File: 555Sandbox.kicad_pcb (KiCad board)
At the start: 2 copper layers, 64.6 x 37 mm, 33 parts, among them J1 VIN, J2 Piezo, SW1 RESET, SW2 MODE, U1 NE555P, U2 LM3914N

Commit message: patch: silkscreen updates
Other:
- board text added: "555"
- board text added: "VOLT- METER"
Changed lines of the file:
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@@
 			(at 4.01 -2.3 180)
 			(layer "F.SilkS")
+			(hide yes)
 			(effects
 				(font
@@
 	(footprint "Potentiometer_THT:Potentiometer_Alps_RK163_Single_Horizontal"
 		(layer "F.Cu")
-		(at 89.6 68.75 -90)
+		(at 89.55 68.75 -90)
 		(descr "1110U1Q 1110TNP 1110U2A 1110U0Q Potentiometer, horizontal, Alps RK163 Single, https://tech.alpsalpine.com/prod/e/pdf/potentiometer/rotarypotentiometers/rk16/rk16.pdf")
 		(tags "Potentiometer horizontal Alps RK163 Single")
@@
 			)
 		)
-		(property ki_fp_filters "Potentiometer*")
-		(sheetname "Root")
-		(sheetfile "555Sandbox.kicad_sch")
 		(attr through_hole)
 		(fp_line
 			(start 6.82 14.07)
-			(end -0.92 14.07)
+			(end -0.72 14.07)
 			(stroke
 				(width 0.12)
@@
 		)
 		(fp_line
-			(start -3.92 11.07)
+			(start -3.92 10.87)
 			(end -3.92 -4.07)
 			(stroke
@@
 		)
 		(fp_arc
-			(start -0.92 14.07)
-			(mid -3.04132 13.19132)
-			(end -3.92 11.07)
+			(start -0.72 14.07)
+			(mid -2.982742 13.132742)
+			(end -3.92 10.87)
 			(stroke
 				(width 0.12)
@@
 	)
 	(gr_line
+		(start 117.725 74.55)
+		(end 117 73.85)
+		(stroke
+			(width 0.25)
+			(type default)
+		)
+		(layer "F.SilkS")
+	)
+	(gr_line
 		(start 113.75 71.65)
 		(end 116.75 71.65)
@@
 	)
 	(gr_line
+		(start 104.85 74.55)
+		(end 102.875 74.55)
+		(stroke
+			(width 0.25)
+			(type default)
+		)
+		(layer "F.SilkS")
+	)
+	(gr_line
 		(start 82.2 72.2)
 		(end 82.2 74.1)
@@
 	)
 	(gr_line
-		(start 110.7 80.1)
-		(end 110.7 90)
+		(start 110.35 80.1)
+		(end 110.35 90)
 		(stroke
 			(width 0.2)
@@
 		(layer "F.SilkS")
 	)
+	(gr_line
+		(start 102.875 74.55)
+		(end 103.6 73.85)
+		(stroke
+			(width 0.25)
+			(type default)
+		)
+		(layer "F.SilkS")
+	)
+	(gr_line
+		(start 102.875 74.55)
+		(end 103.6 75.25)
+		(stroke
+			(width 0.25)
+			(type default)
+		)
+		(layer "F.SilkS")
+	)
 	(gr_arc
 		(start 135.8 65.4)
@@
 	)
 	(gr_line
+		(start 116.2 74.55)
+		(end 117.725 74.55)
+		(stroke
+			(width 0.25)
+			(type default)
+		)
+		(layer "F.SilkS")
+	)
+	(gr_line
 		(start 83.6 72.2)
 		(end 84.3 72.2)
@@
 	)
 	(gr_line
-		(start 110.7 72.8)
-		(end 110.7 76.3)
+		(start 110.35 72.8)
+		(end 110.35 76.3)
 		(stroke
 			(width 0.2)
@@
 		(layer "F.SilkS")
 	)
+	(gr_line
+		(start 117.725 74.55)
+		(end 117 75.25)
+		(stroke
+			(width 0.25)
+			(type default)
+		)
+		(layer "F.SilkS")
+	)
 	(gr_arc
 		(start 139.55 97.5)
@@
 		)
 	)
+	(gr_text "555"
+		(at 109.8375 73.75 0)
+		(layer "F.SilkS")
+		(effects
+			(font
+				(size 1.5 1.5)
+				(thickness 0.3)
+				(bold yes)
+			)
+			(justify right top)
+		)
+	)
 	(gr_text "Freq"
 		(at 84.7 74.1 0)
@@
 		)
 	)
+	(gr_text "VOLT-\nMETER"
+		(at 111 76 0)
+		(layer "F.SilkS")
+		(effects
+			(font
+				(size 1 1)
+				(thickness 0.2)
+				(bold yes)
+			)
+			(justify left bottom)
+		)
+	)
 	(gr_text "5-16V"
 		(at 111 72.3 0)
@@
 	)
 	(segment
+		(start 89.55 68.75)
+		(end 89.55 76.15)
+		(width 1)
+		(layer "F.Cu")
+		(net 4)
+	)
+	(segment
 		(start 102.94 84.54)
 		(end 99.08 84.54)
@@
 	)
 	(segment
-		(start 89.6 68.75)
-		(end 89.6 76.2)
+		(start 89.55 76.15)
+		(end 90.9 77.5)
 		(width 1)
 		(layer "F.Cu")
@@
 	)
 	(segment
-		(start 89.6 76.2)
-		(end 90.9 77.5)
-		(width 1)
-		(layer "F.Cu")
-		(net 4)
-	)
-	(segment
-		(start 84.6 68.75)
+		(start 84.55 68.75)
 		(end 89.6 68.75)
 		(width 1)
@@
 		(end 126.5 70.7)
 		(width 1)
-		(layer "F.Cu")
+		(layer "B.Cu")
 		(net 6)
 	)
@@
 		(end 126.52 75.8)
 		(width 1)
-		(layer "F.Cu")
+		(layer "B.Cu")
 		(net 8)
 	)
@@
 		(end 126.54 80.9)
 		(width 1)
-		(layer "F.Cu")
+		(layer "B.Cu")
 		(net 10)
 	)
@@
 		(end 126.54 85.9)
 		(width 1)
-		(layer "F.Cu")
+		(layer "B.Cu")
 		(net 12)
 	)
@@
 	)
 	(segment
-		(start 129.06 91)
-		(end 126.52 91)
-		(width 1)
-		(layer "F.Cu")
-		(net 14)
-	)
-	(segment
 		(start 126.52 91)
 		(end 126.5 91.02)
@@
 	)
 	(segment
+		(start 129.06 91)
+		(end 126.52 91)
+		(width 1)
+		(layer "B.Cu")
+		(net 14)
+	)
+	(segment
 		(start 95.71 83.4)
 		(end 95.71 87.1)
@@
 	)
 	(segment
-		(start 77 71.35)
-		(end 77 82.85)
+		(start 77 82.85)
+		(end 79.4 85.25)
 		(width 1)
 		(layer "B.Cu")
@@
 	)
 	(segment
-		(start 79.6 68.75)
+		(start 79.55 68.8)
 		(end 77 71.35)
 		(width 1)
@@
 	)
 	(segment
-		(start 77 82.85)
-		(end 79.4 85.25)
+		(start 77 71.35)
+		(end 77 82.85)
+		(width 1)
+		(layer "B.Cu")
+		(net 27)
+	)
+	(segment
+		(start 79.55 68.75)
+		(end 79.55 68.8)
 		(width 1)
 		(layer "B.Cu")

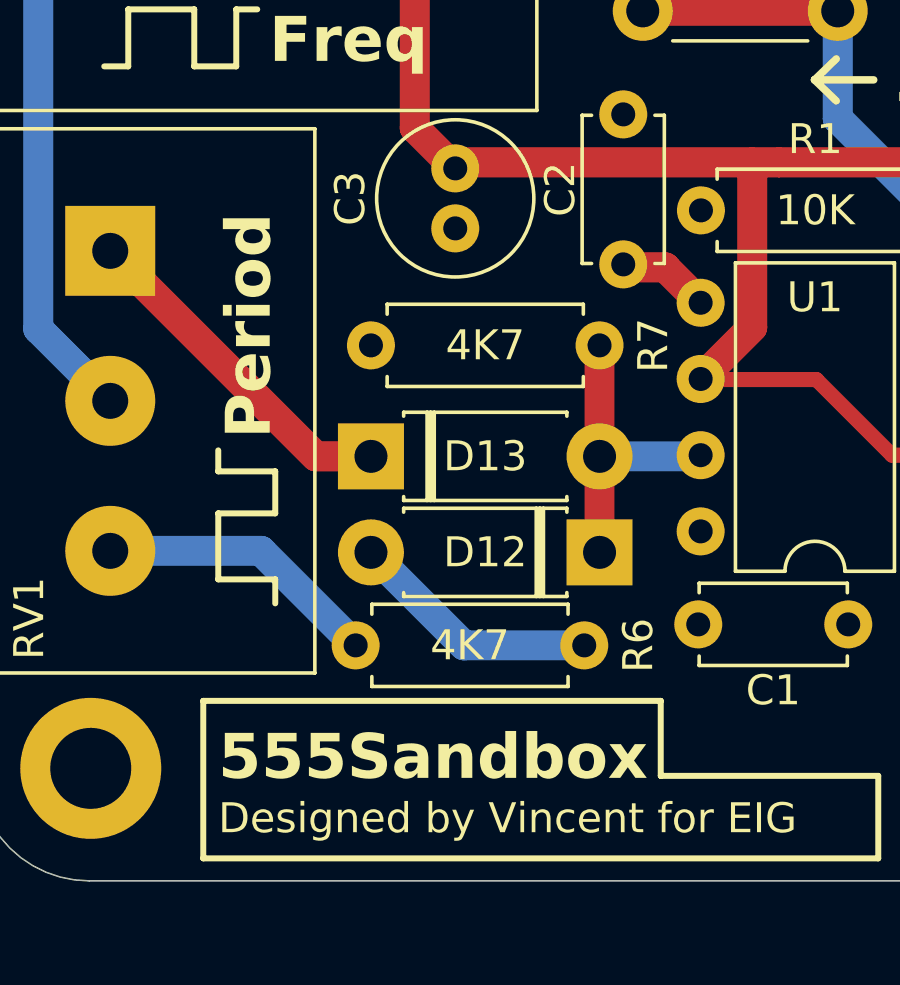
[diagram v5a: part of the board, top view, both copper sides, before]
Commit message: patch: back silkscreen logo additions
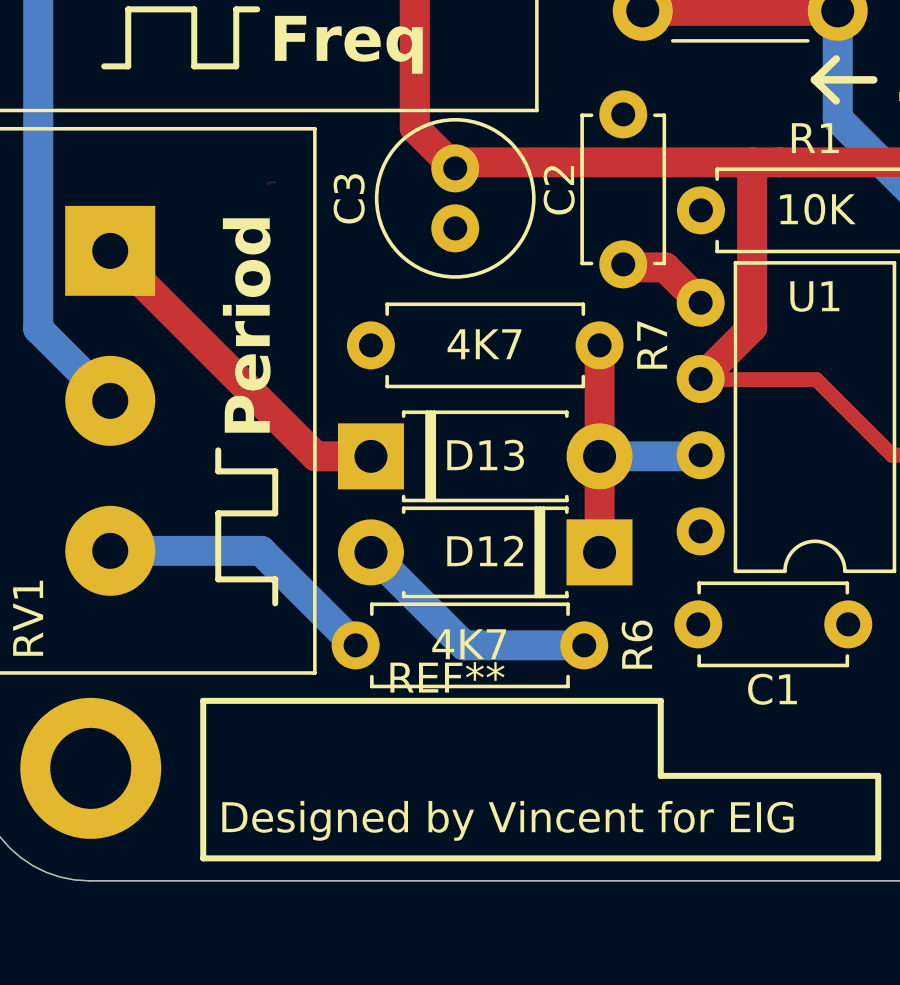
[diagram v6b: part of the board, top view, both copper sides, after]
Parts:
- added G***: LOGO, footprints:Bear_40, F.Cu at (86.5, 80.2)
- added REF**: EIG, footprints:EIG, F.Cu at (90.6, 95.0)

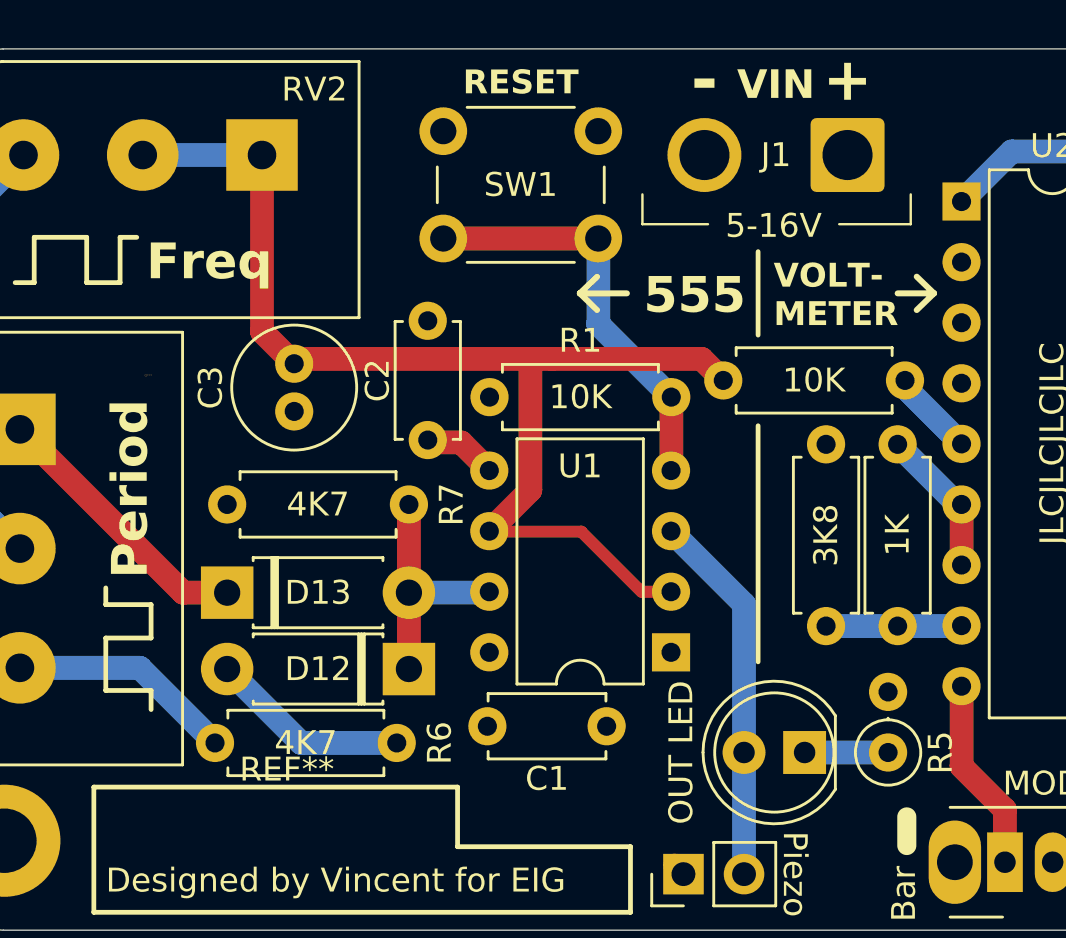
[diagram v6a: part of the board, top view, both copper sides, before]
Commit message: fix: polarised capacitor and erronous silkscreen label
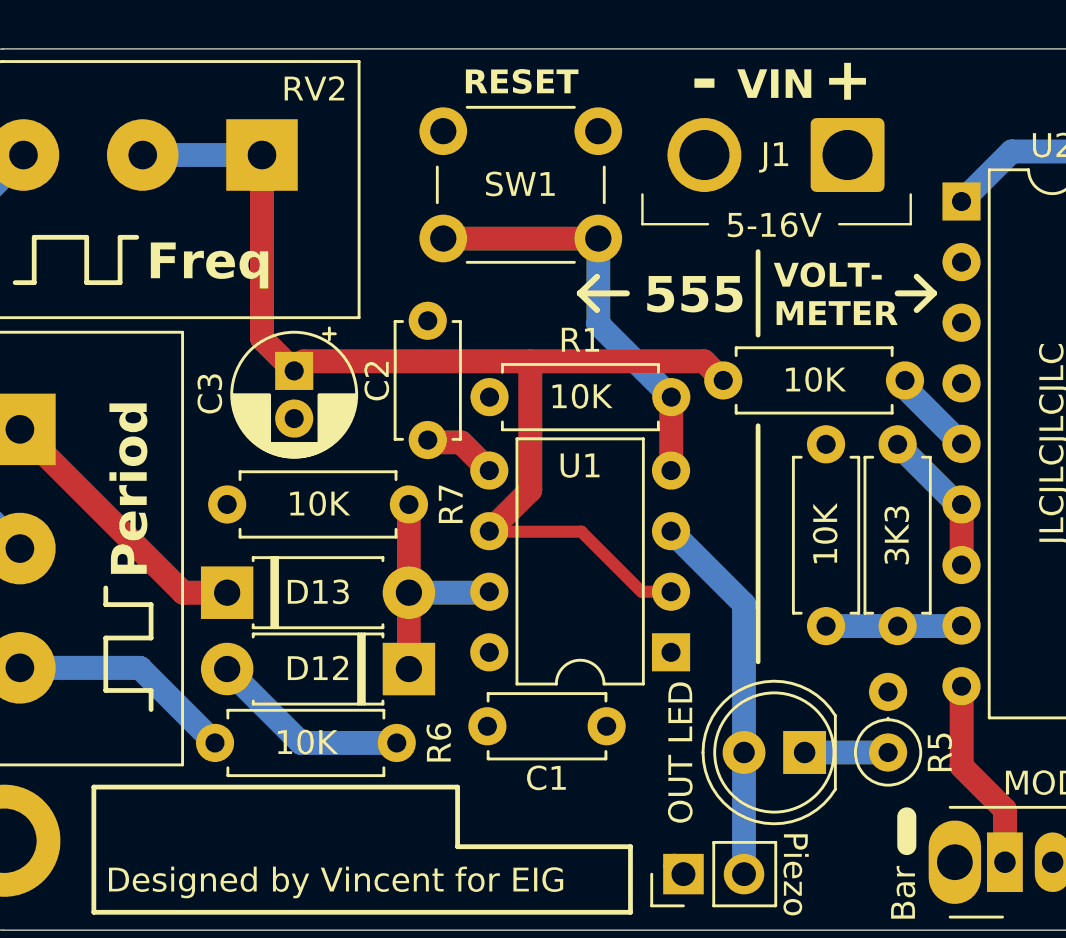
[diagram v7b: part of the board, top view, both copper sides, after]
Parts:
- removed REF**: EIG, footprints:EIG
- C3: footprint Capacitor_THT:C_Radial_D5.0mm_H11.0mm_P2.00mm -> Capacitor_THT:CP_Radial_D5.0mm_P2.00mm
- R2: value 1K -> 3K3
- R4: value 3K8 -> 10K
- R6, R7: value 4K7 -> 10K
- moved C3 0.30 mm to (90.9, 77.8)

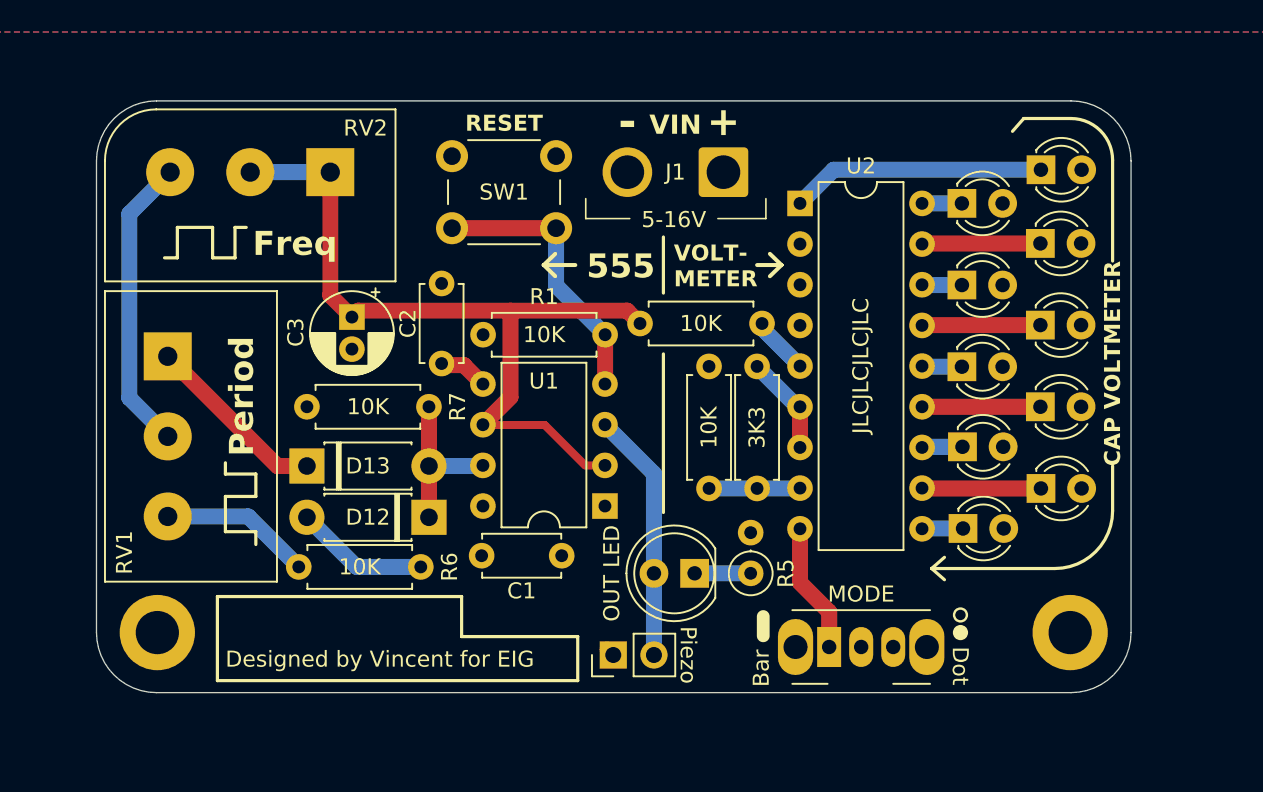
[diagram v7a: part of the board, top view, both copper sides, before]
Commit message: feat: refresh majority of pcb to improve ease of assembly
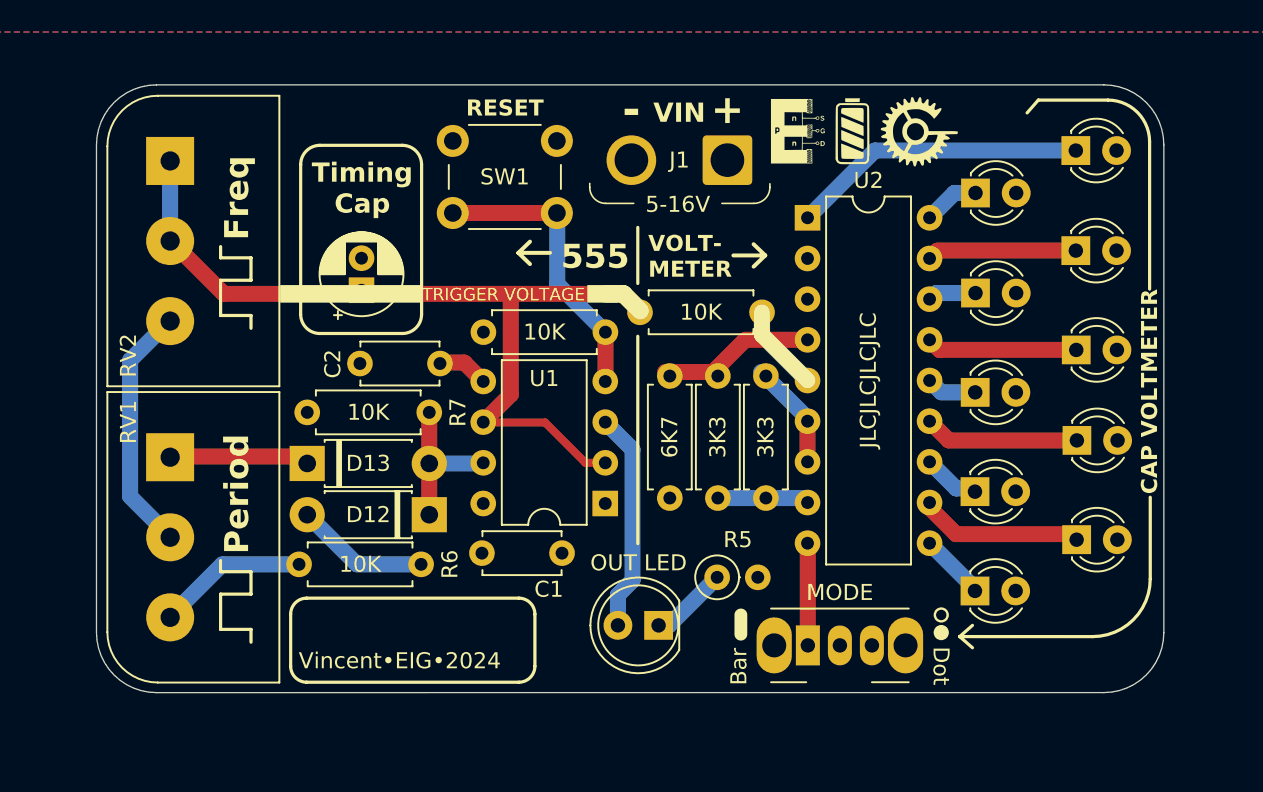
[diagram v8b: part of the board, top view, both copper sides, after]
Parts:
- removed H1, H2: MountingHole_Pad, MountingHole:MountingHole_2.7mm_M2.5_DIN965_Pad
- removed J2: Piezo, Connector_PinHeader_2.54mm:PinHeader_1x02_P2.54mm_Vertical
- added R8: 6K7, Resistor_THT:R_Axial_DIN0207_L6.3mm_D2.5mm_P7.62mm_Horizontal, F.Cu at (110.8, 89.1)
- added REF**: EIG, footprints:EIG, F.Cu at (117.0, 64.2)
- R4: value 10K -> 3K3
- moved RV2 10.0 mm to (79.5, 68.0), turned to 0 degrees
- moved RV1 6.30 mm to (79.5, 86.5)
- moved D11 3.97 mm to (129.8, 94.9)
- moved D1 3.95 mm to (110.0, 97.0)
- moved D10 3.90 mm to (136.2, 91.7)
- moved D8 3.10 mm to (136.2, 85.5)
- moved D9 2.91 mm to (129.8, 88.7)
- moved D6 2.72 mm to (136.1, 79.8)
- moved D2 2.49 mm to (136.1, 67.4)
- moved D4 2.26 mm to (136.1, 73.7)
- moved R5 2.11 mm to (113.7, 94.0), turned to 0 degrees
- moved D7 1.80 mm to (129.8, 82.5)
- moved C3 1.78 mm to (91.5, 76.1), turned to 90 degrees
- moved SW2 1.33 mm to (119.4, 98.3)
- moved D3 1.07 mm to (129.8, 70.0)
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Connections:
- R4 pad 1: GND -> /Voltage Meter/RLO
- U2 pad 4: GND -> /Voltage Meter/RLO
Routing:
- net /Voltage Meter/RLO: track 0.00 -> 9.42 mm
- net /TRIG: track 49.6 -> 53.5 mm
- net Net-(RV1-Pad2): track 18.6 -> 15.6 mm
- net Net-(D10-K): track 7.43 -> 10.3 mm
- net Net-(D12-K): track 11.5 -> 8.74 mm
- net Net-(D2-K): track 15.9 -> 18.5 mm
- net Net-(D8-K): track 7.39 -> 9.70 mm
- net Net-(D6-K): track 7.40 -> 9.42 mm
- net Net-(D4-K): track 7.41 -> 9.34 mm
- net /OUT: track 15.6 -> 13.8 mm
- net Net-(U2-SIG): track 3.64 -> 5.45 mm
- net Net-(SW2A-A): track 8.13 -> 6.39 mm
- net Net-(D11-K): track 2.57 -> 4.01 mm
- net Net-(D1-K): track 3.50 -> 4.90 mm
- net Net-(D3-K): track 2.49 -> 3.51 mm
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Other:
- board size 64.6 x 37 mm -> 66.6 x 38 mm
- board text added: "TRIGGER VOLTAGE"
- board text added: "Timing Cap"
- board text added: "Vincent•EIG•2024"
- board text removed: "Designed by Vincent for EIG"
